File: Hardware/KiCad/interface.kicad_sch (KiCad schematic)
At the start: 10 parts, among them J6 UART, J7 OLED

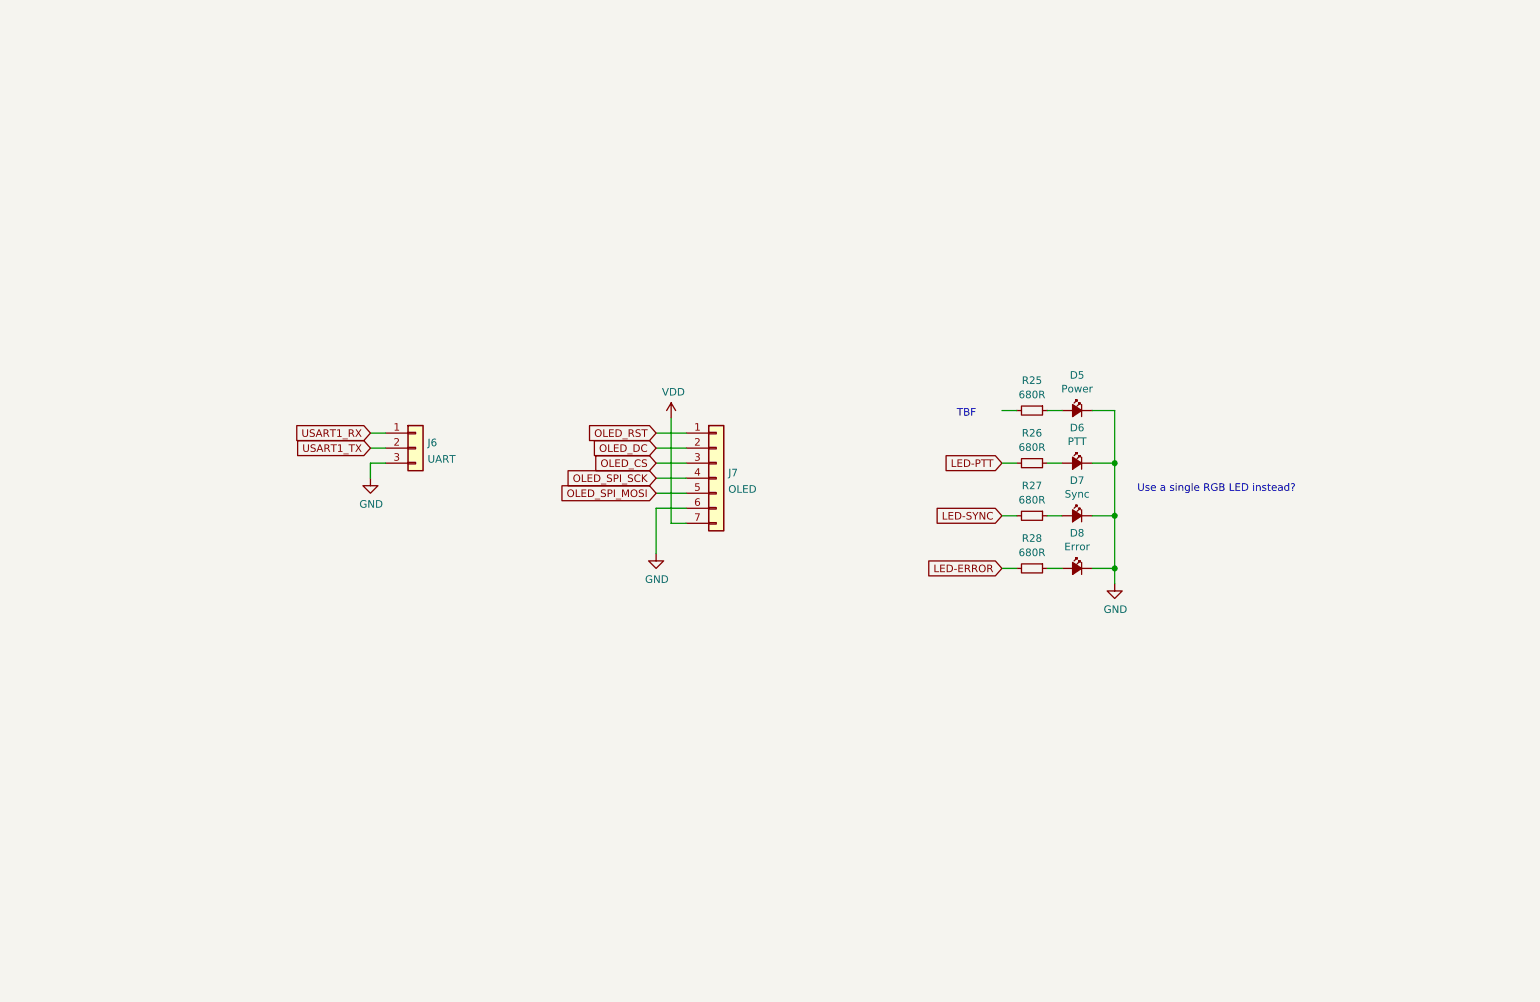
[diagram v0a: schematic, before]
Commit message: Add 4x4 keyboard
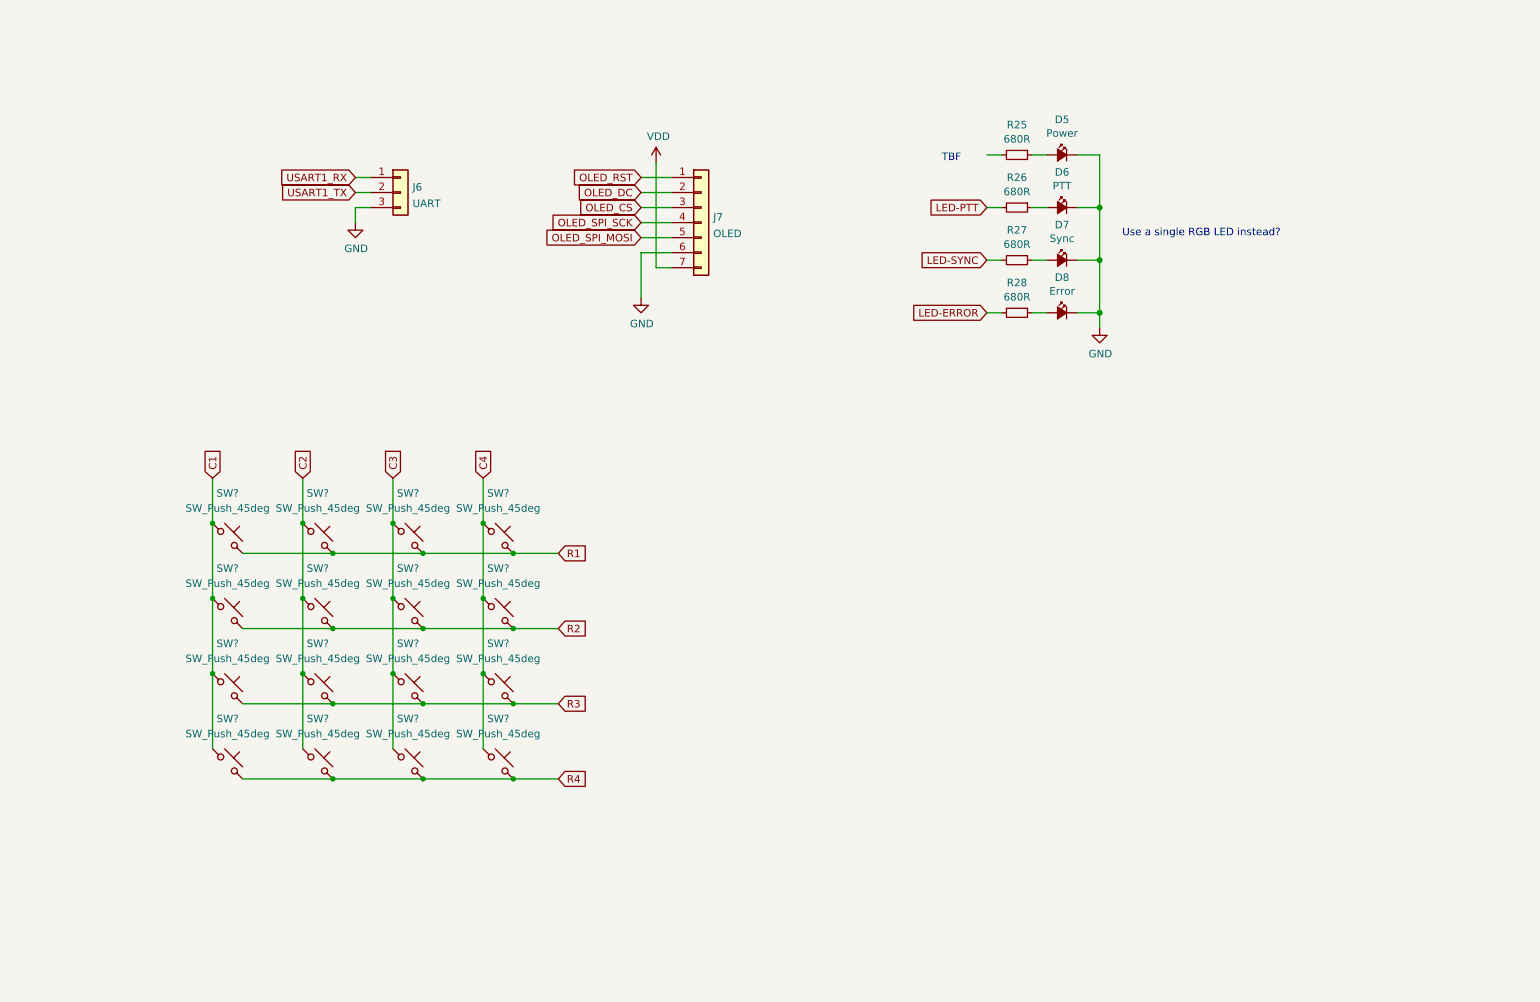
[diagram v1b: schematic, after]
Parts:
- added SW? (x16): SW_Push_45deg, Button_Switch_SMD:SW_Push_1P1T_NO_CK_KMR2, symbol Switch:SW_Push_45deg
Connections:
- new net C1: SW?.1, SW?.1, SW?.1, SW?.1
- new net C2: SW?.1, SW?.1, SW?.1, SW?.1
- new net C3: SW?.1, SW?.1, SW?.1, SW?.1
- new net C4: SW?.1, SW?.1, SW?.1, SW?.1
- new net R1: SW?.2, SW?.2, SW?.2, SW?.2
- new net R2: SW?.2, SW?.2, SW?.2, SW?.2
- new net R3: SW?.2, SW?.2, SW?.2, SW?.2
- new net R4: SW?.2, SW?.2, SW?.2, SW?.2
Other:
- moved on the sheet: D5, D6, D7, D8, J6, J7, R25, R26, R27, R28

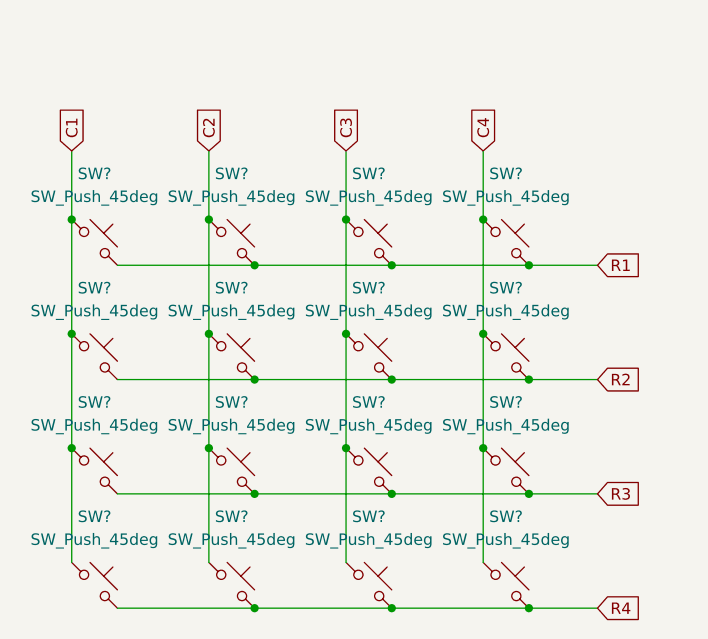
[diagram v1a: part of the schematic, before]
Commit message: Add decoupling capacitors and fix issue #7
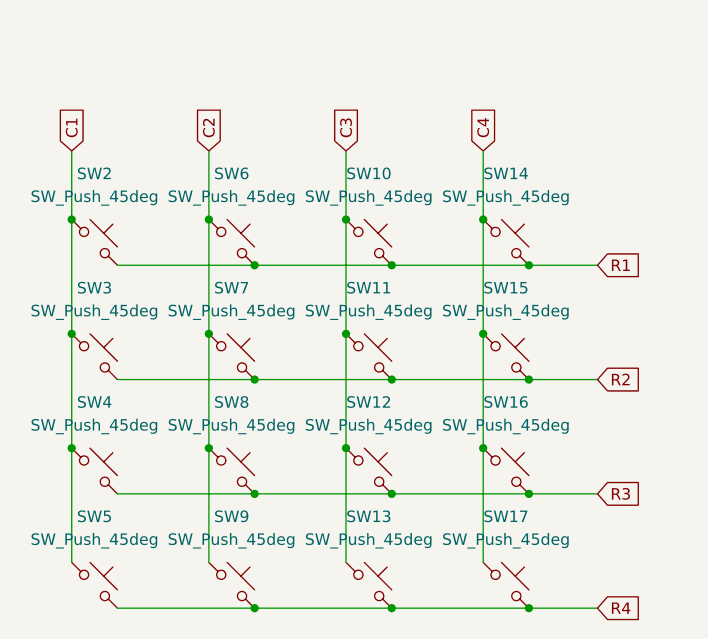
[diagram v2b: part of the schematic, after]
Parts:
- gave numbers to parts that had none: 16
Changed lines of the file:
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@@
   (symbol (lib_id "Switch:SW_Push_45deg") (at 58.42 124.46 0) (unit 1)
     (in_bom yes) (on_board yes) (fields_autoplaced)
-    (property "Reference" "SW?" (id 0) (at 58.42 116.84 0))
+    (property "Reference" "SW3" (id 0) (at 58.42 116.84 0))
     (property "Value" "SW_Push_45deg" (id 1) (at 58.42 119.38 0))
     (property "Footprint" "Button_Switch_SMD:SW_Push_1P1T_NO_CK_KMR2" (id 2) (at 58.42 124.46 0)
@@
   (symbol (lib_id "Switch:SW_Push_45deg") (at 104.14 137.16 0) (unit 1)
     (in_bom yes) (on_board yes) (fields_autoplaced)
-    (property "Reference" "SW?" (id 0) (at 104.14 129.54 0))
+    (property "Reference" "SW16" (id 0) (at 104.14 129.54 0))
     (property "Value" "SW_Push_45deg" (id 1) (at 104.14 132.08 0))
     (property "Footprint" "Button_Switch_SMD:SW_Push_1P1T_NO_CK_KMR2" (id 2) (at 104.14 137.16 0)
@@
   (symbol (lib_id "Switch:SW_Push_45deg") (at 73.66 124.46 0) (unit 1)
     (in_bom yes) (on_board yes) (fields_autoplaced)
-    (property "Reference" "SW?" (id 0) (at 73.66 116.84 0))
+    (property "Reference" "SW7" (id 0) (at 73.66 116.84 0))
     (property "Value" "SW_Push_45deg" (id 1) (at 73.66 119.38 0))
     (property "Footprint" "Button_Switch_SMD:SW_Push_1P1T_NO_CK_KMR2" (id 2) (at 73.66 124.46 0)
@@
   (symbol (lib_id "Switch:SW_Push_45deg") (at 88.9 111.76 0) (unit 1)
     (in_bom yes) (on_board yes) (fields_autoplaced)
-    (property "Reference" "SW?" (id 0) (at 88.9 104.14 0))
+    (property "Reference" "SW10" (id 0) (at 88.9 104.14 0))
     (property "Value" "SW_Push_45deg" (id 1) (at 88.9 106.68 0))
     (property "Footprint" "Button_Switch_SMD:SW_Push_1P1T_NO_CK_KMR2" (id 2) (at 88.9 111.76 0)
@@
   (symbol (lib_id "Switch:SW_Push_45deg") (at 104.14 149.86 0) (unit 1)
     (in_bom yes) (on_board yes) (fields_autoplaced)
-    (property "Reference" "SW?" (id 0) (at 104.14 142.24 0))
+    (property "Reference" "SW17" (id 0) (at 104.14 142.24 0))
     (property "Value" "SW_Push_45deg" (id 1) (at 104.14 144.78 0))
     (property "Footprint" "Button_Switch_SMD:SW_Push_1P1T_NO_CK_KMR2" (id 2) (at 104.14 149.86 0)
@@
   (symbol (lib_id "Switch:SW_Push_45deg") (at 88.9 149.86 0) (unit 1)
     (in_bom yes) (on_board yes) (fields_autoplaced)
-    (property "Reference" "SW?" (id 0) (at 88.9 142.24 0))
+    (property "Reference" "SW13" (id 0) (at 88.9 142.24 0))
     (property "Value" "SW_Push_45deg" (id 1) (at 88.9 144.78 0))
     (property "Footprint" "Button_Switch_SMD:SW_Push_1P1T_NO_CK_KMR2" (id 2) (at 88.9 149.86 0)
@@
   (symbol (lib_id "Switch:SW_Push_45deg") (at 104.14 124.46 0) (unit 1)
     (in_bom yes) (on_board yes) (fields_autoplaced)
-    (property "Reference" "SW?" (id 0) (at 104.14 116.84 0))
+    (property "Reference" "SW15" (id 0) (at 104.14 116.84 0))
     (property "Value" "SW_Push_45deg" (id 1) (at 104.14 119.38 0))
     (property "Footprint" "Button_Switch_SMD:SW_Push_1P1T_NO_CK_KMR2" (id 2) (at 104.14 124.46 0)
@@
   (symbol (lib_id "Switch:SW_Push_45deg") (at 104.14 111.76 0) (unit 1)
     (in_bom yes) (on_board yes) (fields_autoplaced)
-    (property "Reference" "SW?" (id 0) (at 104.14 104.14 0))
+    (property "Reference" "SW14" (id 0) (at 104.14 104.14 0))
     (property "Value" "SW_Push_45deg" (id 1) (at 104.14 106.68 0))
     (property "Footprint" "Button_Switch_SMD:SW_Push_1P1T_NO_CK_KMR2" (id 2) (at 104.14 111.76 0)
@@
   (symbol (lib_id "Switch:SW_Push_45deg") (at 88.9 124.46 0) (unit 1)
     (in_bom yes) (on_board yes) (fields_autoplaced)
-    (property "Reference" "SW?" (id 0) (at 88.9 116.84 0))
+    (property "Reference" "SW11" (id 0) (at 88.9 116.84 0))
     (property "Value" "SW_Push_45deg" (id 1) (at 88.9 119.38 0))
     (property "Footprint" "Button_Switch_SMD:SW_Push_1P1T_NO_CK_KMR2" (id 2) (at 88.9 124.46 0)
@@
   (symbol (lib_id "Switch:SW_Push_45deg") (at 58.42 149.86 0) (unit 1)
     (in_bom yes) (on_board yes) (fields_autoplaced)
-    (property "Reference" "SW?" (id 0) (at 58.42 142.24 0))
+    (property "Reference" "SW5" (id 0) (at 58.42 142.24 0))
     (property "Value" "SW_Push_45deg" (id 1) (at 58.42 144.78 0))
     (property "Footprint" "Button_Switch_SMD:SW_Push_1P1T_NO_CK_KMR2" (id 2) (at 58.42 149.86 0)
@@
   (symbol (lib_id "Switch:SW_Push_45deg") (at 58.42 137.16 0) (unit 1)
     (in_bom yes) (on_board yes) (fields_autoplaced)
-    (property "Reference" "SW?" (id 0) (at 58.42 129.54 0))
+    (property "Reference" "SW4" (id 0) (at 58.42 129.54 0))
     (property "Value" "SW_Push_45deg" (id 1) (at 58.42 132.08 0))
     (property "Footprint" "Button_Switch_SMD:SW_Push_1P1T_NO_CK_KMR2" (id 2) (at 58.42 137.16 0)
@@
   (symbol (lib_id "Switch:SW_Push_45deg") (at 73.66 149.86 0) (unit 1)
     (in_bom yes) (on_board yes) (fields_autoplaced)
-    (property "Reference" "SW?" (id 0) (at 73.66 142.24 0))
+    (property "Reference" "SW9" (id 0) (at 73.66 142.24 0))
     (property "Value" "SW_Push_45deg" (id 1) (at 73.66 144.78 0))
     (property "Footprint" "Button_Switch_SMD:SW_Push_1P1T_NO_CK_KMR2" (id 2) (at 73.66 149.86 0)
@@
   (symbol (lib_id "Switch:SW_Push_45deg") (at 58.42 111.76 0) (unit 1)
     (in_bom yes) (on_board yes) (fields_autoplaced)
-    (property "Reference" "SW?" (id 0) (at 58.42 104.14 0))
+    (property "Reference" "SW2" (id 0) (at 58.42 104.14 0))
     (property "Value" "SW_Push_45deg" (id 1) (at 58.42 106.68 0))
     (property "Footprint" "Button_Switch_SMD:SW_Push_1P1T_NO_CK_KMR2" (id 2) (at 58.42 111.76 0)
@@
   (symbol (lib_id "Switch:SW_Push_45deg") (at 88.9 137.16 0) (unit 1)
     (in_bom yes) (on_board yes) (fields_autoplaced)
-    (property "Reference" "SW?" (id 0) (at 88.9 129.54 0))
+    (property "Reference" "SW12" (id 0) (at 88.9 129.54 0))
     (property "Value" "SW_Push_45deg" (id 1) (at 88.9 132.08 0))
     (property "Footprint" "Button_Switch_SMD:SW_Push_1P1T_NO_CK_KMR2" (id 2) (at 88.9 137.16 0)
@@
   (symbol (lib_id "Switch:SW_Push_45deg") (at 73.66 137.16 0) (unit 1)
     (in_bom yes) (on_board yes) (fields_autoplaced)
-    (property "Reference" "SW?" (id 0) (at 73.66 129.54 0))
+    (property "Reference" "SW8" (id 0) (at 73.66 129.54 0))
     (property "Value" "SW_Push_45deg" (id 1) (at 73.66 132.08 0))
     (property "Footprint" "Button_Switch_SMD:SW_Push_1P1T_NO_CK_KMR2" (id 2) (at 73.66 137.16 0)
@@
   (symbol (lib_id "Switch:SW_Push_45deg") (at 73.66 111.76 0) (unit 1)
     (in_bom yes) (on_board yes) (fields_autoplaced)
-    (property "Reference" "SW?" (id 0) (at 73.66 104.14 0))
+    (property "Reference" "SW6" (id 0) (at 73.66 104.14 0))
     (property "Value" "SW_Push_45deg" (id 1) (at 73.66 106.68 0))
     (property "Footprint" "Button_Switch_SMD:SW_Push_1P1T_NO_CK_KMR2" (id 2) (at 73.66 111.76 0)
